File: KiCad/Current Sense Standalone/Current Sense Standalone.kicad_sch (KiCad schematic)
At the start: 11 parts, among them J1 PLUG INPUT BATTERY IN HERE (X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, J3 V+/- TEST Header PIN, J4 BAT +TERMINAL TEST HEADER PIN, J5 HEADER PIN FOR TEST, J6 to MCU GPIO PIN, J7 PLUG BATTERY OUTPUT HERE (XT6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, U1 INA139QPWRQ1

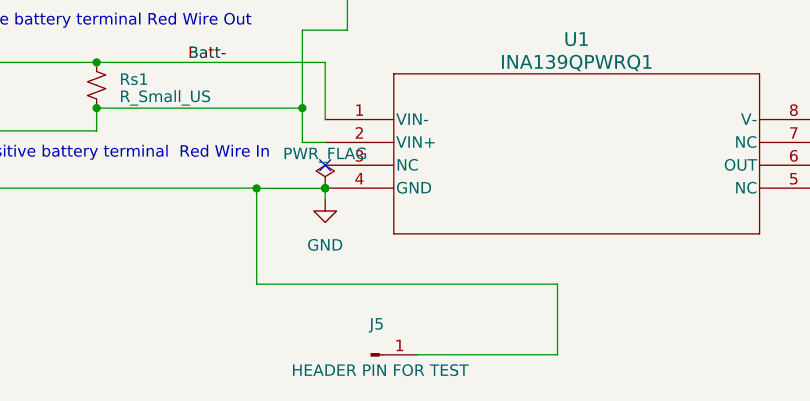
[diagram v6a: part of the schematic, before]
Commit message: Mill Current Sense PCB
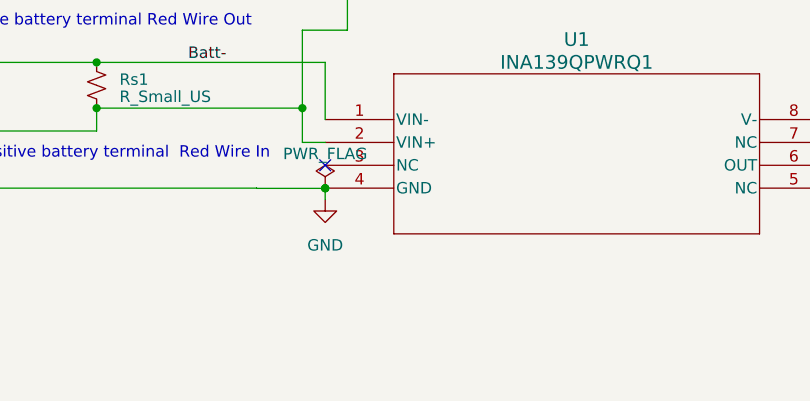
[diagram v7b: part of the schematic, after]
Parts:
- removed J5: HEADER PIN FOR TEST, Connector_PinHeader_2.54mm:PinHeader_1x02_P2.54mm_Vertical, symbol Connector:Conn_01x01_Pin
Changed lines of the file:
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@@
   (junction (at 201.93 49.8856) (diameter 0) (color 0 0 0 0)
   )
-  (junction (at 138.43 94.006) (diameter 0) (color 0 0 0 0)
-  )
   (junction (at 226.06 91.44) (diameter 0) (color 0 0 0 0)
   )
@@
     (stroke (width 0) (type default))
   )
-  (wire (pts (xy 156.2293 112.505) (xy 156.2293 112.4966))
-    (stroke (width 0) (type default))
-  )
   (wire (pts (xy 226.06 102.87) (xy 226.06 105.41))
     (stroke (width 0) (type default))
   )
-  (wire (pts (xy 138.43 104.648) (xy 138.43 94.006))
-    (stroke (width 0) (type default))
-  )
   (wire (pts (xy 120.65 85.09) (xy 143.51 85.09))
     (stroke (width 0) (type default))
@@
     (stroke (width 0) (type default))
   )
-  (wire (pts (xy 156.2293 112.4966) (xy 171.8564 112.4966))
-    (stroke (width 0) (type default))
-  )
   (wire (pts (xy 226.06 91.44) (xy 250.19 91.44))
     (stroke (width 0) (type default))
@@
     (stroke (width 0) (type default))
   )
-  (wire (pts (xy 138.43 104.648) (xy 171.8564 104.648))
-    (stroke (width 0) (type default))
-  )
   (wire (pts (xy 148.5138 76.4286) (xy 148.5138 48.1076))
     (stroke (width 0) (type default))
@@
     (stroke (width 0) (type default))
   )
-  (wire (pts (xy 171.8564 104.648) (xy 171.8564 112.4966))
-    (stroke (width 0) (type default))
-  )
   (wire (pts (xy 175.5902 52.4073) (xy 175.5902 54.9402))
     (stroke (width 0) (type default))
@@
         )
       )
-    )
-  )
-  (symbol (lib_id "Connector:Conn_01x01_Pin") (at 151.1493 112.505 0) (unit 1)
-    (in_bom yes) (on_board yes) (dnp no)
-    (property "Reference" "J5" (at 151.7843 109.1014 0)
-      (effects (font (size 1.27 1.27)))
-    )
-    (property "Value" "HEADER PIN FOR TEST" (at 152.146 114.2492 0)
-      (effects (font (size 1.27 1.27)))
-    )
-    (property "Footprint" "Connector_PinHeader_2.54mm:PinHeader_1x02_P2.54mm_Vertical" (at 151.1493 112.505 0)
-      (effects (font (size 1.27 1.27)) hide)
-    )
-    (property "Datasheet" "~" (at 151.1493 112.505 0)
-      (effects (font (size 1.27 1.27)) hide)
-    )
-    (pin "1")
-    (instances
-      (project "Current Sense Standalone"
-        (path "/af3dddb2-191c-40a1-9395-0fad50eefcf8"
-          (reference "J5") (unit 1)
-        )
-      )

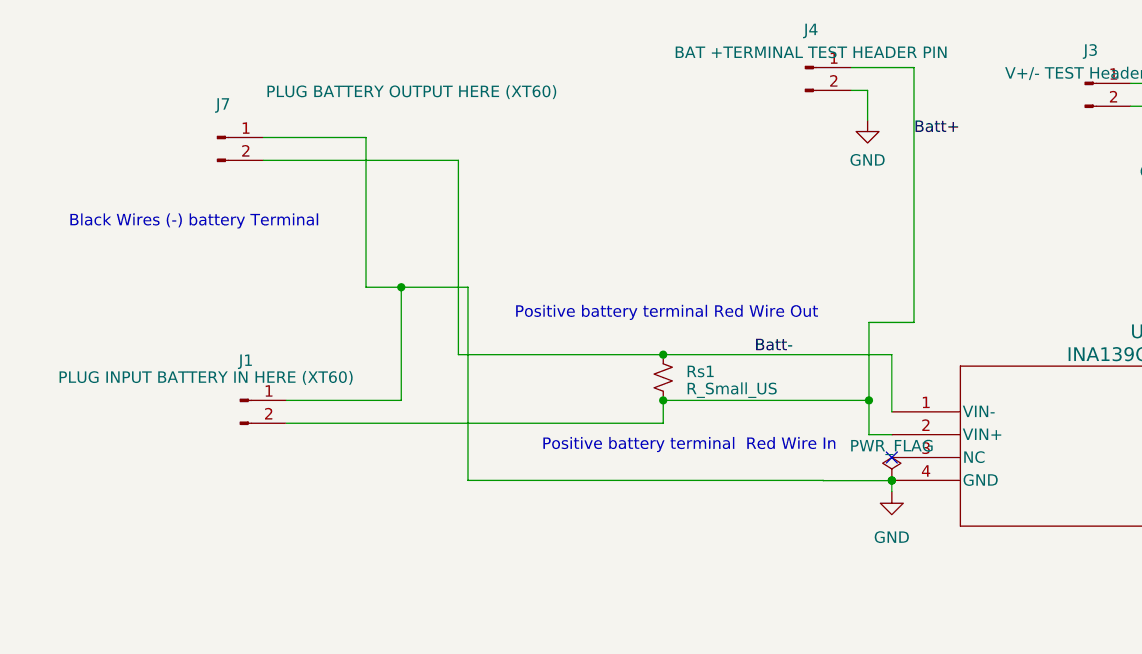
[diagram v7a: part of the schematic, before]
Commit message: rearranged schematic for current sense
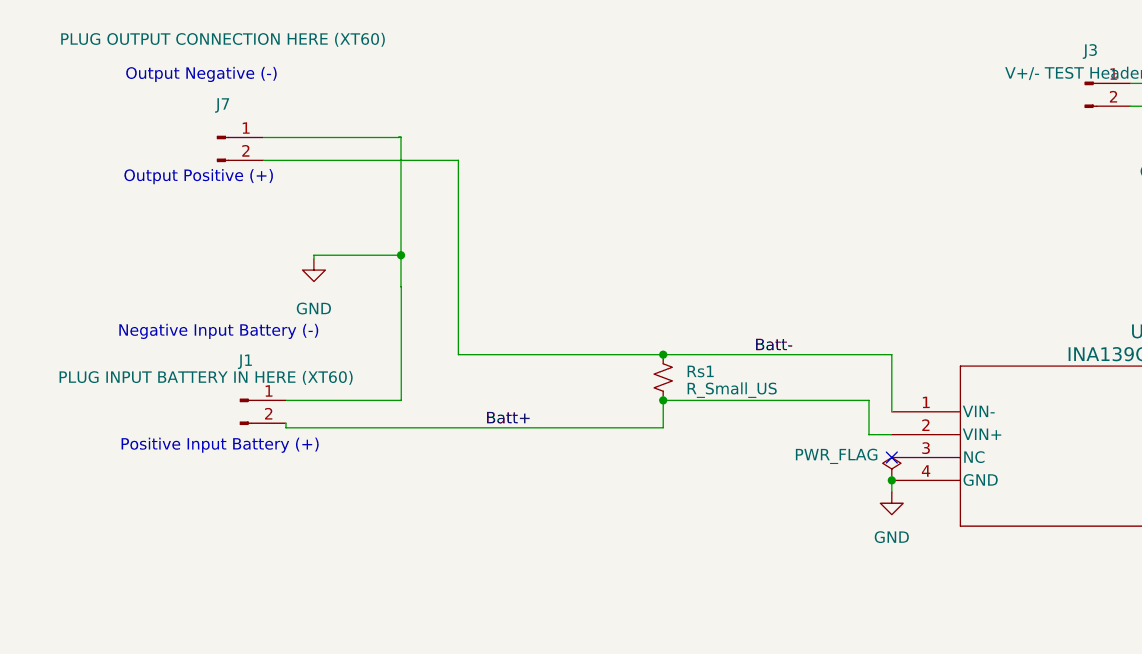
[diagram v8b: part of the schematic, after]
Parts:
- removed J4: BAT +TERMINAL TEST HEADER PIN, Connector_PinHeader_2.54mm:PinHeader_1x02_P2.54mm_Vertical, symbol Connector:Conn_01x02_Pin
- J7: value PLUG BATTERY OUTPUT HERE (XT60) -> PLUG OUTPUT CONNECTION HERE (XT60)
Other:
- note added: "Negative Input Battery (-)"
- note added: "Output Negative (-)"
- note added: "Output Positive (+)"
- note added: "Positive Input Battery (+)"
- note removed: "Black Wires (-) battery Terminal"
- note removed: "Positive battery terminal Red Wire In"
- note removed: "Positive battery terminal Red Wire Out"
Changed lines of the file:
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@@
   (junction (at 120.65 80.01) (diameter 0) (color 0 0 0 0)
   )
-  (junction (at 146.05 94.006) (diameter 0) (color 0 0 0 0)
+  (junction (at 91.5162 68.9609) (diameter 0) (color 0 0 0 0)
   )
   (junction (at 146.05 93.98) (diameter 0) (color 0 0 0 0)
@@
   (junction (at 226.06 91.44) (diameter 0) (color 0 0 0 0)
   )
-  (junction (at 91.5454 72.517) (diameter 0) (color 0 0 0 0)
-  )
   (junction (at 201.93 86.36) (diameter 0) (color 0 0 0 0)
   )
@@
   (junction (at 210.82 91.44) (diameter 0) (color 0 0 0 0)
   )
-  (junction (at 143.51 85.09) (diameter 0) (color 0 0 0 0)
-  )
   (no_connect (at 146.05 91.44))
   (no_connect (at 201.93 88.9))
   (no_connect (at 201.93 93.98))
-  (wire (pts (xy 146.05 80.01) (xy 146.05 86.36))
-    (stroke (width 0) (type default))
-  )
-  (wire (pts (xy 120.65 80.01) (xy 146.05 80.01))
+  (wire (pts (xy 91.2876 55.88) (xy 76.2 55.88))
     (stroke (width 0) (type default))
   )
-  (wire (pts (xy 138.43 93.98) (xy 138.43 94.006))
+  (wire (pts (xy 146.05 80.01) (xy 146.05 86.36))
     (stroke (width 0) (type default))
   )
-  (wire (pts (xy 143.51 76.4286) (xy 143.51 85.09))
+  (wire (pts (xy 120.65 80.01) (xy 146.05 80.01))
     (stroke (width 0) (type default))
   )
@@
     (stroke (width 0) (type default))
   )
-  (wire (pts (xy 138.43 94.006) (xy 146.05 94.006))
-    (stroke (width 0) (type default))
-  )
   (wire (pts (xy 226.06 91.44) (xy 250.19 91.44))
     (stroke (width 0) (type default))
@@
     (stroke (width 0) (type default))
   )
-  (wire (pts (xy 76.2 55.88) (xy 87.63 55.88))
+  (wire (pts (xy 91.2876 55.8292) (xy 91.5162 55.8292))
     (stroke (width 0) (type default))
   )
@@
     (stroke (width 0) (type default))
   )
-  (wire (pts (xy 201.93 49.8673) (xy 201.93 49.8856))
+  (wire (pts (xy 78.74 88.138) (xy 120.65 88.138))
     (stroke (width 0) (type default))
   )
-  (wire (pts (xy 236.7788 85.9252) (xy 236.7788 86.8426))
+  (wire (pts (xy 91.5162 68.9609) (xy 91.5162 72.4662))
     (stroke (width 0) (type default))
   )
-  (wire (pts (xy 141.5288 50.6476) (xy 143.3576 50.6476))
+  (wire (pts (xy 201.93 49.8673) (xy 201.93 49.8856))
     (stroke (width 0) (type default))
   )
-  (wire (pts (xy 146.05 95.25) (xy 146.05 94.006))
+  (wire (pts (xy 91.2876 55.8292) (xy 91.2876 55.88))
+    (stroke (width 0) (type default))
+  )
+  (wire (pts (xy 236.7788 85.9252) (xy 236.7788 86.8426))
     (stroke (width 0) (type default))
   )
@@
     (stroke (width 0) (type default))
   )
-  (wire (pts (xy 91.5454 72.517) (xy 98.9584 72.517))
+  (wire (pts (xy 91.5162 55.8292) (xy 91.5162 68.9609))
     (stroke (width 0) (type default))
   )
-  (wire (pts (xy 87.63 55.88) (xy 87.63 72.517))
+  (wire (pts (xy 81.8388 68.9609) (xy 81.8388 69.342))
     (stroke (width 0) (type default))
   )
@@
     (stroke (width 0) (type default))
   )
-  (wire (pts (xy 120.65 87.63) (xy 120.65 85.09))
+  (wire (pts (xy 120.65 85.09) (xy 120.65 88.138))
     (stroke (width 0) (type default))
   )
-  (wire (pts (xy 143.3576 50.6476) (xy 143.3576 53.9496))
+  (wire (pts (xy 91.5162 72.4662) (xy 91.5454 72.4662))
     (stroke (width 0) (type default))
   )
-  (wire (pts (xy 87.63 72.517) (xy 91.5454 72.517))
+  (wire (pts (xy 91.5162 68.9609) (xy 81.8388 68.9609))
     (stroke (width 0) (type default))
   )
@@
     (stroke (width 0) (type default))
   )
-  (wire (pts (xy 148.5138 76.4286) (xy 148.5138 48.1076))
-    (stroke (width 0) (type default))
-  )
   (wire (pts (xy 97.8916 80.01) (xy 120.65 80.01))
     (stroke (width 0) (type default))
   )
-  (wire (pts (xy 98.9584 72.517) (xy 98.9584 93.98))
-    (stroke (width 0) (type default))
-  )
   (wire (pts (xy 172.6111 49.8673) (xy 201.93 49.8673))
     (stroke (width 0) (type default))
@@
     (stroke (width 0) (type default))
   )
-  (wire (pts (xy 91.5454 85.09) (xy 91.5454 72.517))
+  (wire (pts (xy 91.5454 72.4662) (xy 91.5454 85.09))
     (stroke (width 0) (type default))
   )
@@
     (stroke (width 0) (type default))
   )
-  (wire (pts (xy 148.5138 48.1076) (xy 141.5288 48.1076))
+  (wire (pts (xy 78.74 88.138) (xy 78.74 87.63))
     (stroke (width 0) (type default))
   )
-  (wire (pts (xy 146.05 94.006) (xy 146.05 93.98))
+  (wire (pts (xy 146.05 93.98) (xy 146.05 95.25))
     (stroke (width 0) (type default))
   )
@@
     (stroke (width 0) (type default))
   )
-  (wire (pts (xy 98.9584 93.98) (xy 138.43 93.98))
-    (stroke (width 0) (type default))
-  )
-  (wire (pts (xy 78.74 87.63) (xy 120.65 87.63))
-    (stroke (width 0) (type default))
-  )
   (wire (pts (xy 76.2 58.42) (xy 97.8916 58.42))
     (stroke (width 0) (type default))
   )
-  (wire (pts (xy 148.5138 76.4286) (xy 143.51 76.4286))
-    (stroke (width 0) (type default))
-  )
   (wire (pts (xy 228.8553 83.4136) (xy 250.19 83.4136))
     (stroke (width 0) (type default))
@@
     (effects (font (size 1.27 1.27)) (justify left bottom))
   )
+  (text "Positive Input Battery (+)\n" (at 60.2996 90.9574 0)
+    (effects (font (size 1.27 1.27)) (justify left bottom))
+  )
   (text "-Negative (GND) Signal for Microcontroller to read current"
     (at 201.803 46.609 0)
     (effects (font (size 1.27 1.27)) (justify left bottom))
   )
-  (text "Positive battery terminal  Red Wire In" (at 107.1626 90.8812 0)
+  (text "Output Negative (-)" (at 60.8838 49.7586 0)
     (effects (font (size 1.27 1.27)) (justify left bottom))
   )
-  (text "Black Wires (-) battery Terminal" (at 54.61 66.04 0)
+  (text "Output Positive (+)" (at 60.6806 61.1124 0)
     (effects (font (size 1.27 1.27)) (justify left bottom))
   )
-  (text "Positive battery terminal Red Wire Out" (at 104.14 76.2 0)
+  (text "Negative Input Battery (-)\n" (at 60.0456 78.3082 0)
     (effects (font (size 1.27 1.27)) (justify left bottom))
   )
@@
     (effects (font (size 1.27 1.27)) (justify left bottom))
   )
-  (label "Batt+" (at 148.5138 55.755 0) (fields_autoplaced)
+  (label "Batt+" (at 100.9142 88.138 0) (fields_autoplaced)
     (effects (font (size 1.27 1.27)) (justify left bottom))
   )
@@
   )
   (symbol (lib_id "power:PWR_FLAG") (at 146.05 93.98 0) (unit 1)
-    (in_bom yes) (on_board yes) (dnp no) (fields_autoplaced)
+    (in_bom yes) (on_board yes) (dnp no)
     (property "Reference" "#FLG01" (at 146.05 92.075 0)
       (effects (font (size 1.27 1.27)) hide)
     )
-    (property "Value" "PWR_FLAG" (at 146.05 90.17 0)
+    (property "Value" "PWR_FLAG" (at 139.9032 91.1606 0)
       (effects (font (size 1.27 1.27)))
     )
@@
       (effects (font (size 1.27 1.27)))
     )
-    (property "Value" "PLUG BATTERY OUTPUT HERE (XT60)" (at 92.71 50.8 0)
+    (property "Value" "PLUG OUTPUT CONNECTION HERE (XT60)" (at 71.7296 44.9834 0)
       (effects (font (size 1.27 1.27)))
     )
@@
     )
   )
+  (symbol (lib_id "power:GND") (at 81.8388 69.342 0) (unit 1)
+    (in_bom yes) (on_board yes) (dnp no) (fields_autoplaced)
+    (property "Reference" "#PWR08" (at 81.8388 75.692 0)
+      (effects (font (size 1.27 1.27)) hide)
+    )
+    (property "Value" "GND" (at 81.8388 74.93 0)
+      (effects (font (size 1.27 1.27)))
+    )
+    (property "Footprint" "" (at 81.8388 69.342 0)
+      (effects (font (size 1.27 1.27)) hide)
+    )
+    (property "Datasheet" "" (at 81.8388 69.342 0)
+      (effects (font (size 1.27 1.27)) hide)
+    )
+    (pin "1")
+    (instances
+      (project "Current Sense Standalone"
+        (path "/af3dddb2-191c-40a1-9395-0fad50eefcf8"
+          (reference "#PWR08") (unit 1)
+        )
+      )
+    )
+  )
   (symbol (lib_id "Device:C_Small") (at 226.06 100.33 0) (unit 1)
     (in_bom yes) (on_board yes) (dnp no) (fields_autoplaced)
@@
     )
   )
-  (symbol (lib_id "Connector:Conn_01x02_Pin") (at 136.4488 48.1076 0) (unit 1)
-    (in_bom yes) (on_board yes) (dnp no) (fields_autoplaced)
-    (property "Reference" "J4" (at 137.0838 43.9166 0)
-      (effects (font (size 1.27 1.27)))
-    )
-    (property "Value" "BAT +TERMINAL TEST HEADER PIN" (at 137.0838 46.4566 0)
-      (effects (font (size 1.27 1.27)))
-    )
-    (property "Footprint" "Connector_PinHeader_2.54mm:PinHeader_1x02_P2.54mm_Vertical" (at 136.4488 48.1076 0)
-      (effects (font (size 1.27 1.27)) hide)
-    )
-    (property "Datasheet" "~" (at 136.4488 48.1076 0)
-      (effects (font (size 1.27 1.27)) hide)
-    )
-    (pin "1")
-    (pin "2")
-    (instances
-      (project "Current Sense Standalone"
-        (path "/af3dddb2-191c-40a1-9395-0fad50eefcf8"
-          (reference "J4") (unit 1)
-        )
-      )
-    )
-  )
   (symbol (lib_id "power:GND") (at 236.7788 86.8426 0) (unit 1)
     (in_bom yes) (on_board yes) (dnp no) (fields_autoplaced)
@@
         )
       )
-    )
-  )
-  (symbol (lib_id "power:GND") (at 143.3576 53.9496 0) (unit 1)
-    (in_bom yes) (on_board yes) (dnp no) (fields_autoplaced)
-    (property "Reference" "#PWR04" (at 143.3576 60.2996 0)
-      (effects (font (size 1.27 1.27)) hide)
-    )
-    (property "Value" "GND" (at 143.3576 58.42 0)
-      (effects (font (size 1.27 1.27)))
-    )
-    (property "Footprint" "" (at 143.3576 53.9496 0)
-      (effects (font (size 1.27 1.27)) hide)
-    )
-    (property "Datasheet" "" (at 143.3576 53.9496 0)
-      (effects (font (size 1.27 1.27)) hide)
-    )
-    (pin "1")
-    (instances
-      (project "Current Sense Standalone"
-        (path "/af3dddb2-191c-40a1-9395-0fad50eefcf8"
-          (reference "#PWR04") (unit 1)
-        )
-      )
